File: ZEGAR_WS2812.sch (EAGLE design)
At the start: 151 parts, among them IC2 DS3231/SO, IC3 ATMEGA328P, Q2 MMBT3906LT1SMD, Q3 MMBT3906LT1SMD, Q4 MMBT3906LT1SMD, Q5 MMBT3906LT1SMD, U1 SN74HC595D, U10 SN74HC595D, U2 SN74HC595D, U3 SN74HC595D, U4 SN74HC595D, U5 SN74HC595D, U6 SN74HC595D, U7 SN74HC595D, U8 SN74HC595D, U9 SN74HC595D

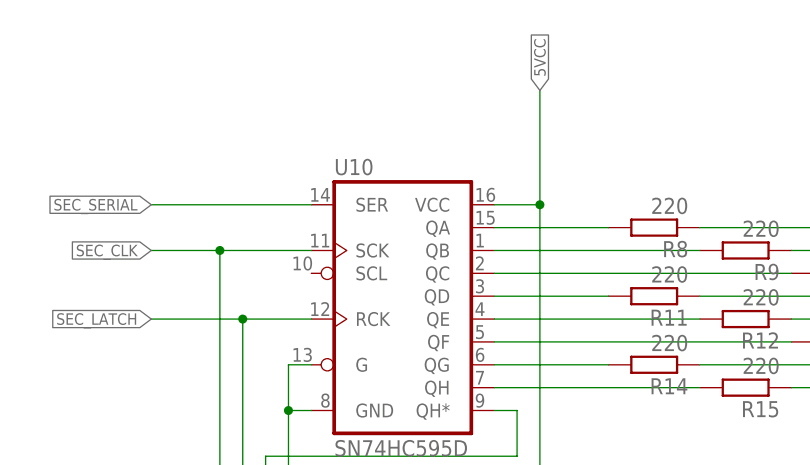
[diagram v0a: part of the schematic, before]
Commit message: placed traces from diodes to shift registers
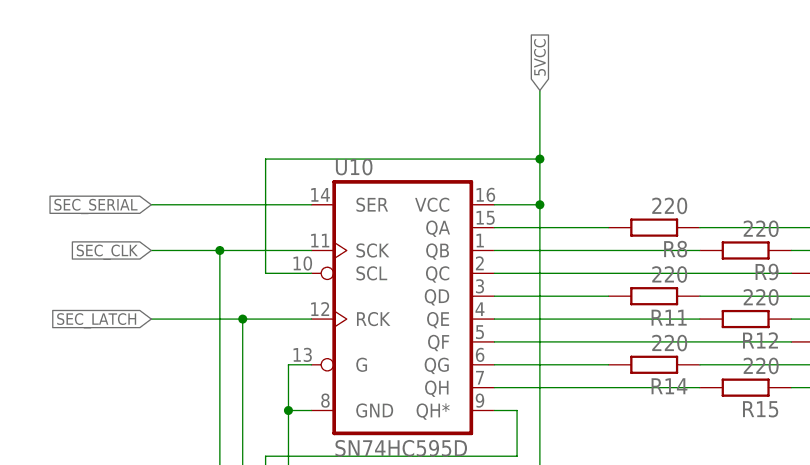
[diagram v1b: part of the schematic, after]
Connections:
- net 5VCC: now also U10.SCL
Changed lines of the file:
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@@
 <wire x1="226.06" y1="254" x2="231.14" y2="254" width="0.1524" layer="91"/>
 <junction x="231.14" y="254"/>
-<wire x1="231.14" y1="330.2" x2="231.14" y2="342.9" width="0.1524" layer="91"/>
+<wire x1="231.14" y1="330.2" x2="231.14" y2="335.28" width="0.1524" layer="91"/>
 <junction x="231.14" y="330.2"/>
 <label x="231.14" y="342.9" size="1.27" layer="95" rot="R90" xref="yes"/>
+<pinref part="U10" gate="U1" pin="SCL"/>
+<wire x1="231.14" y1="335.28" x2="231.14" y2="342.9" width="0.1524" layer="91"/>
+<wire x1="205.74" y1="322.58" x2="200.66" y2="322.58" width="0.1524" layer="91"/>
+<wire x1="200.66" y1="322.58" x2="200.66" y2="335.28" width="0.1524" layer="91"/>
+<wire x1="200.66" y1="335.28" x2="231.14" y2="335.28" width="0.1524" layer="91"/>
+<junction x="231.14" y="335.28"/>
 </segment>
 </net>

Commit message: hc595 for seconds completed
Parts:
- removed JP3: (no value), pinhead:PINHD-1X7
- added C10, C11, C12, C5, C6, C7, C8, C9: 100n, rcl:C-EUC0805
- added R68, R72, R77, R78, R79, R80, R81: 0, rcl:R-EU_R2512
- added R69, R70, R71, R73, R74, R75, R76: 0, rcl:R-EU_R1206
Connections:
- removed net N$3: U3.SER, U9.QH*
- new net N$133: U9.QH*
- new net SEC_SER: U3.SER
- net 4DIG_1IN: now also U1.QC; no longer U2.QC
- net 4DIG_2IN: now also U1.QD; no longer U2.QD
- net 4DIG_3IN: now also U1.QE; no longer U2.QE
- net 4DIG_4IN: now also U1.QB; no longer U2.QB
- net 4DIG_A: now also U1.QH; no longer U2.QH
- net 4DIG_B: now also U1.QF; no longer U2.QF
- net 4DIG_C: now also U2.QG; no longer U1.QE
- net 4DIG_D: now also U2.QE; no longer U1.QC
- net 4DIG_DP: now also U2.QF; no longer U1.QD
- net 4DIG_E: now also U2.QD; no longer U1.QB
- net 4DIG_F: now also U1.QG; no longer U2.QG
- net 4DIG_G: now also U2.QH; no longer U1.QF
- net 5VCC: now also C10.2, C11.2, C12.2, C5.1, C6.1, C7.1, C8.1, C9.1, R68.1, R68.2, R72.1, R72.2, R77.1, R77.2, R78.1, R78.2, R79.1, R79.2, R80.1, R80.2, R81.1, R81.2
- net GND: now also C10.1, C11.1, C12.1, C5.2, C6.2, C7.2, C8.2, C9.2
- net SEC_CLK: now also R69.1, R69.2, R70.1, R70.2, R71.1, R71.2, R73.1, R73.2, R74.1, R74.2
- net SEC_LATCH: now also R75.1, R75.2, R76.1, R76.2
- net SEC_SERIAL: now also U8.QH*
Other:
- moved on the sheet: C3, D1, D10, D11, D12, D13, D14, D15, D16, D2, D3, D4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

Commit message: almost done
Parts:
- removed R7: 0, rcl:R-EU_R0805
- added R82, R83, R87: 0, rcl:R-EU_R2512
- added R84, R85, R86, R88: 1k, Resistor:RCHIP-0805(2012-METRIC)
- added S1, S2, S3, S4: (no value), switch-omron:10-XX
- added U$1: TP4056-PTH, 32teeth - TP4056 Module:TP4056-PTH
- R6: device rcl:R-EU_R0805 -> rcl:R-EU_R2512
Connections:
- new net BUTTONS: IC3.PC2(ADC2/PCINT10), R84.2, R87.1, R87.2, R88.1, S1.P, S1.P1
- new net N$138: R84.1, R85.2, S2.P, S2.P1
- new net N$139: R85.1, R86.2, S3.P, S3.P1
- new net N$140: R86.1, S4.P, S4.P1
- net 4DIG_CLK: now also IC3.PB1(PCINT1/OC1A); no longer IC3.PB5(SCK/PCINT5)
- net 4DIG_LATCH: now also IC3.PB0(PCINT0/CLKO/ICP1), R83.1, R83.2; no longer IC3.PB4(PCINT4/MISO), R6.1, R6.2
- net 4DIG_SER: now also IC3.PB2(PCINT2/!SS!/OC1B); no longer IC3.PB3(PCINT3/OC2A/MOSI)
- net 5VCC: now also R6.1, R6.2, R82.1, R82.2, R88.2
- net GND: now also S1.S, S1.S1, S2.S, S2.S1, S3.S, S3.S1, S4.S, S4.S1; no longer R7.1, R7.2
- net SEC_CLK: now also IC3.PD6(PCINT22/OC0A/AIN0)
- net SEC_LATCH: now also IC3.PD7(PCINT23/AIN1)
- net SEC_SER: now also IC3.PD5(PCINT21/OC0B/T1)
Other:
- moved on the sheet: C1, C10, C11, C12, C2, IC3, Q1, R1, R6

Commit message: done?
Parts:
- removed U$1: TP4056-PTH, 32teeth - TP4056 Module:TP4056-PTH
- added JP3: (no value), pinhead-2:PINHD-2X03_2.54-SMD
- added R7: 0, rcl:R-EU_R1206
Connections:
- new net MISO: IC3.PB4(PCINT4/MISO), JP3.1
- new net MOSI: IC3.PB3(PCINT3/OC2A/MOSI), JP3.4
- new net SCK: IC3.PB5(SCK/PCINT5), JP3.3
- net 5VCC: now also JP3.2
- net GND: now also JP3.6, R7.1, R7.2
- net RESET: now also JP3.5
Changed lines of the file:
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@@
 <part name="S4" library="switch-omron" library_urn="urn:adsk.eagle:library:377" deviceset="10-XX" device="" package3d_urn="urn:adsk.eagle:package:27496/1"/>
 <part name="R87" library="rcl" library_urn="urn:adsk.eagle:library:334" deviceset="R-EU_" device="R2512" package3d_urn="urn:adsk.eagle:package:23545/2" value="0"/>
-<part name="U$1" library="32teeth - TP4056 Module" deviceset="TP4056-PTH" device=""/>
+<part name="R7" library="rcl" library_urn="urn:adsk.eagle:library:334" deviceset="R-EU_" device="R1206" package3d_urn="urn:adsk.eagle:package:23540/2" value="0"/>
+<part name="JP3" library="pinhead-2" deviceset="PINHD-2X03" device="_2.54-SMD"/>
 </parts>
 <sheets>
@@
 <attribute name="VALUE" x="80.01" y="264.922" size="1.778" layer="96" rot="R180"/>
 </instance>
-<instance part="U$1" gate="G$1" x="40.64" y="0" smashed="yes"/>
+<instance part="R7" gate="G$1" x="33.02" y="-15.24" smashed="yes" rot="R180">
+<attribute name="NAME" x="36.83" y="-16.7386" size="1.778" layer="95" rot="R180"/>
+<attribute name="VALUE" x="36.83" y="-11.938" size="1.778" layer="96" rot="R180"/>
+</instance>
+<instance part="JP3" gate="A" x="45.72" y="93.98" smashed="yes">
+<attribute name="NAME" x="39.37" y="99.695" size="1.778" layer="95"/>
+<attribute name="VALUE" x="39.37" y="86.36" size="1.778" layer="96"/>
+</instance>
 </instances>
 <busses>
@@
 <junction x="104.14" y="261.62"/>
 </segment>
+<segment>
+<pinref part="R7" gate="G$1" pin="1"/>
+<wire x1="22.86" y1="-2.54" x2="20.32" y2="-2.54" width="0.1524" layer="91"/>
+<wire x1="22.86" y1="-15.24" x2="22.86" y2="-2.54" width="0.1524" layer="91"/>
+<wire x1="27.94" y1="-15.24" x2="22.86" y2="-15.24" width="0.1524" layer="91"/>
+<label x="20.32" y="-2.54" size="1.27" layer="95" rot="R180" xref="yes"/>
+<pinref part="R7" gate="G$1" pin="2"/>
+<wire x1="27.94" y1="-15.24" x2="38.1" y2="-15.24" width="0.1524" layer="91"/>
+<junction x="27.94" y="-15.24"/>
+<wire x1="22.86" y1="-2.54" x2="40.64" y2="-2.54" width="0.1524" layer="91"/>
+<wire x1="40.64" y1="-2.54" x2="40.64" y2="-15.24" width="0.1524" layer="91"/>
+<junction x="22.86" y="-2.54"/>
+<wire x1="40.64" y1="-15.24" x2="38.1" y2="-15.24" width="0.1524" layer="91"/>
+<junction x="38.1" y="-15.24"/>
+</segment>
+<segment>
+<pinref part="JP3" gate="A" pin="6"/>
+<wire x1="50.8" y1="91.44" x2="58.42" y2="91.44" width="0.1524" layer="91"/>
+<wire x1="58.42" y1="91.44" x2="58.42" y2="81.28" width="0.1524" layer="91"/>
+<wire x1="58.42" y1="81.28" x2="53.34" y2="81.28" width="0.1524" layer="91"/>
+<label x="53.34" y="81.28" size="1.27" layer="95" rot="R180" xref="yes"/>
+</segment>
 </net>
 <net name="XTAL1" class="0">
@@
 <label x="83.82" y="276.86" size="1.27" layer="95" rot="R90" xref="yes"/>
 </segment>
+<segment>
+<pinref part="JP3" gate="A" pin="2"/>
+<wire x1="50.8" y1="96.52" x2="58.42" y2="96.52" width="0.1524" layer="91"/>
+<wire x1="58.42" y1="96.52" x2="58.42" y2="106.68" width="0.1524" layer="91"/>
+<wire x1="58.42" y1="106.68" x2="50.8" y2="106.68" width="0.1524" layer="91"/>
+<label x="50.8" y="106.68" size="1.27" layer="95" rot="R180" xref="yes"/>
+</segment>
 </net>
 <net name="SCL" class="0">
@@
 <pinref part="R1" gate="G$1" pin="1"/>
 <wire x1="149.86" y1="83.82" x2="152.4" y2="83.82" width="0.1524" layer="91"/>
+</segment>
+<segment>
+<pinref part="JP3" gate="A" pin="5"/>
+<wire x1="43.18" y1="91.44" x2="35.56" y2="91.44" width="0.1524" layer="91"/>
+<wire x1="35.56" y1="91.44" x2="35.56" y2="81.28" width="0.1524" layer="91"/>
+<wire x1="35.56" y1="81.28" x2="38.1" y2="81.28" width="0.1524" layer="91"/>
+<label x="38.1" y="81.28" size="1.27" layer="95" xref="yes"/>
 </segment>
 </net>
@@
 </segment>
 </net>
+<net name="MOSI" class="0">
+<segment>
+<pinref part="IC3" gate="G$1" pin="PB3(PCINT3/OC2A/MOSI)"/>
+<wire x1="83.82" y1="99.06" x2="55.88" y2="99.06" width="0.1524" layer="91"/>
+<wire x1="55.88" y1="99.06" x2="55.88" y2="93.98" width="0.1524" layer="91"/>
+<pinref part="JP3" gate="A" pin="4"/>
+<wire x1="55.88" y1="93.98" x2="50.8" y2="93.98" width="0.1524" layer="91"/>
+<label x="73.66" y="99.06" size="1.27" layer="95" rot="R180" xref="yes"/>
+</segment>
+</net>
+<net name="MISO" class="0">
+<segment>
+<pinref part="IC3" gate="G$1" pin="PB4(PCINT4/MISO)"/>
+<wire x1="83.82" y1="93.98" x2="60.96" y2="93.98" width="0.1524" layer="91"/>
+<pinref part="JP3" gate="A" pin="1"/>
+<wire x1="43.18" y1="96.52" x2="38.1" y2="96.52" width="0.1524" layer="91"/>
+<wire x1="38.1" y1="96.52" x2="38.1" y2="101.6" width="0.1524" layer="91"/>
+<wire x1="38.1" y1="101.6" x2="60.96" y2="101.6" width="0.1524" layer="91"/>
+<wire x1="60.96" y1="101.6" x2="60.96" y2="93.98" width="0.1524" layer="91"/>
+<label x="38.1" y="96.52" size="1.27" layer="95" rot="R180" xref="yes"/>
+</segment>
+</net>
+<net name="SCK" class="0">
+<segment>
+<pinref part="IC3" gate="G$1" pin="PB5(SCK/PCINT5)"/>
+<wire x1="83.82" y1="88.9" x2="63.5" y2="88.9" width="0.1524" layer="91"/>
+<pinref part="JP3" gate="A" pin="3"/>
+<wire x1="43.18" y1="93.98" x2="38.1" y2="93.98" width="0.1524" layer="91"/>
+<wire x1="38.1" y1="93.98" x2="38.1" y2="86.36" width="0.1524" layer="91"/>
+<wire x1="38.1" y1="86.36" x2="63.5" y2="86.36" width="0.1524" layer="91"/>
+<wire x1="63.5" y1="86.36" x2="63.5" y2="88.9" width="0.1524" layer="91"/>
+<label x="38.1" y="93.98" size="1.27" layer="95" rot="R180" xref="yes"/>
+</segment>
+</net>

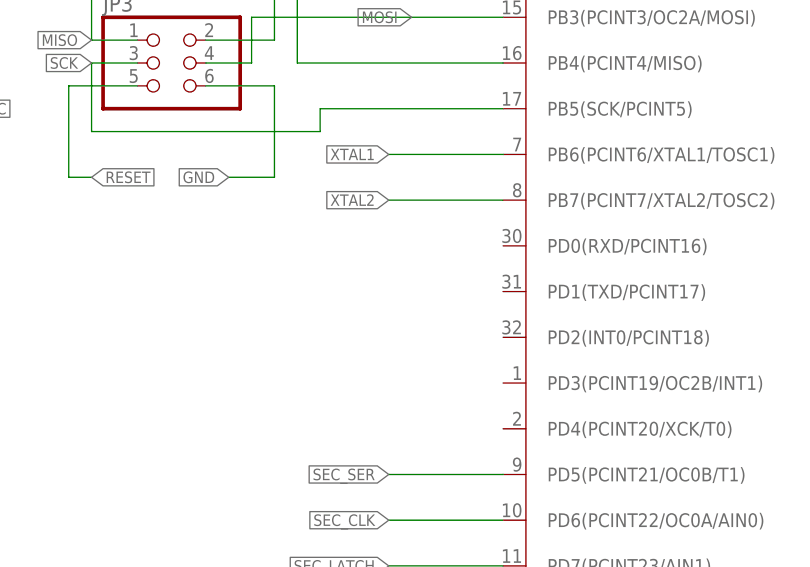
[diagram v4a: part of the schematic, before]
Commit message: added programming pins and rx tx pins
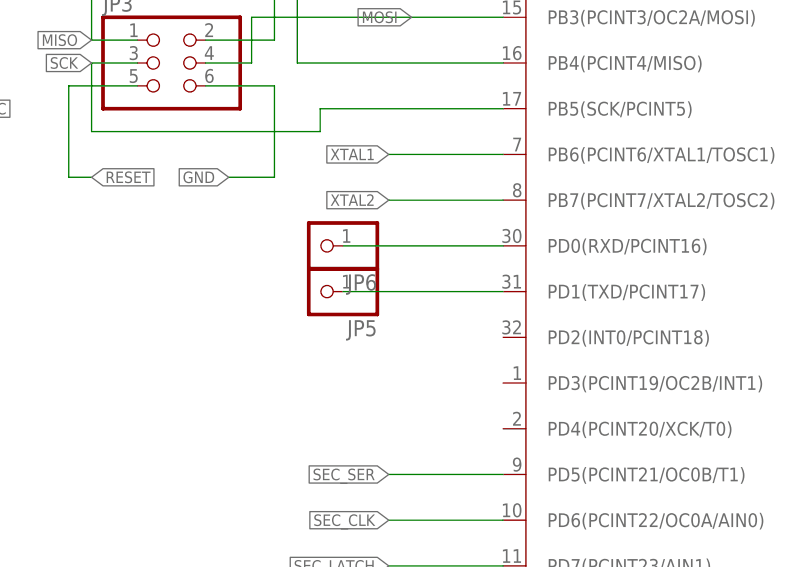
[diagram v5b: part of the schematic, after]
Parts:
- added JP5, JP6: (no value), pinhead-2:PINHD-1X01_2.54-SMD-90°
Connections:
- new net N$135: IC3.PD0(RXD/PCINT16), JP6.1
- new net N$136: IC3.PD1(TXD/PCINT17), JP5.1
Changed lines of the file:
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@@
 <part name="R7" library="rcl" library_urn="urn:adsk.eagle:library:334" deviceset="R-EU_" device="R1206" package3d_urn="urn:adsk.eagle:package:23540/2" value="0"/>
 <part name="JP3" library="pinhead-2" deviceset="PINHD-2X03" device="_2.54-SMD"/>
+<part name="JP5" library="pinhead-2" deviceset="PINHD-1X01" device="_2.54-SMD-90°"/>
+<part name="JP6" library="pinhead-2" deviceset="PINHD-1X01" device="_2.54-SMD-90°"/>
 </parts>
 <sheets>
@@
 <attribute name="VALUE" x="39.37" y="86.36" size="1.778" layer="96"/>
 </instance>
+<instance part="JP5" gate="A" x="63.5" y="68.58" smashed="yes" rot="R180">
+<attribute name="NAME" x="69.85" y="65.405" size="1.778" layer="95" rot="R180"/>
+<attribute name="VALUE" x="69.85" y="73.66" size="1.778" layer="96" rot="R180"/>
+</instance>
+<instance part="JP6" gate="A" x="63.5" y="73.66" smashed="yes" rot="R180">
+<attribute name="NAME" x="69.85" y="70.485" size="1.778" layer="95" rot="R180"/>
+<attribute name="VALUE" x="69.85" y="78.74" size="1.778" layer="96" rot="R180"/>
+</instance>
 </instances>
 <busses>
@@
 </segment>
 </net>
+<net name="N$135" class="0">
+<segment>
+<wire x1="66.04" y1="73.66" x2="83.82" y2="73.66" width="0.1524" layer="91"/>
+<pinref part="IC3" gate="G$1" pin="PD0(RXD/PCINT16)"/>
+<pinref part="JP6" gate="A" pin="1"/>
+</segment>
+</net>
+<net name="N$136" class="0">
+<segment>
+<pinref part="IC3" gate="G$1" pin="PD1(TXD/PCINT17)"/>
+<wire x1="83.82" y1="68.58" x2="66.04" y2="68.58" width="0.1524" layer="91"/>
+<pinref part="JP5" gate="A" pin="1"/>
+</segment>
+</net>
